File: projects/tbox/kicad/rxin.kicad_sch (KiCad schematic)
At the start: 24 parts, among them U601 OPA1678

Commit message: Annotate by board: KiCad annotator, first free after sheet number x100 (1xxx front, 2xxx control, 3xxx rear)
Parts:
- renumbered C601 to C3401, C602 to C3402, C618 to C3403, C619 to C3404, C622 to C3405, C623 to C3406, C614 to C3407, R601 to R3401, R605 to R3402, R635 to R3403, R636 to R3404, R602 to R3405, R606 to R3406, R633 to R3407, R634 to R3408, R603 to R3409, R607 to R3410, R604 to R3411, R608 to R3412, RV601 to RV3401, RV602 to RV3402, TP601 to TP3401, TP602 to TP3402, U601 to U3401

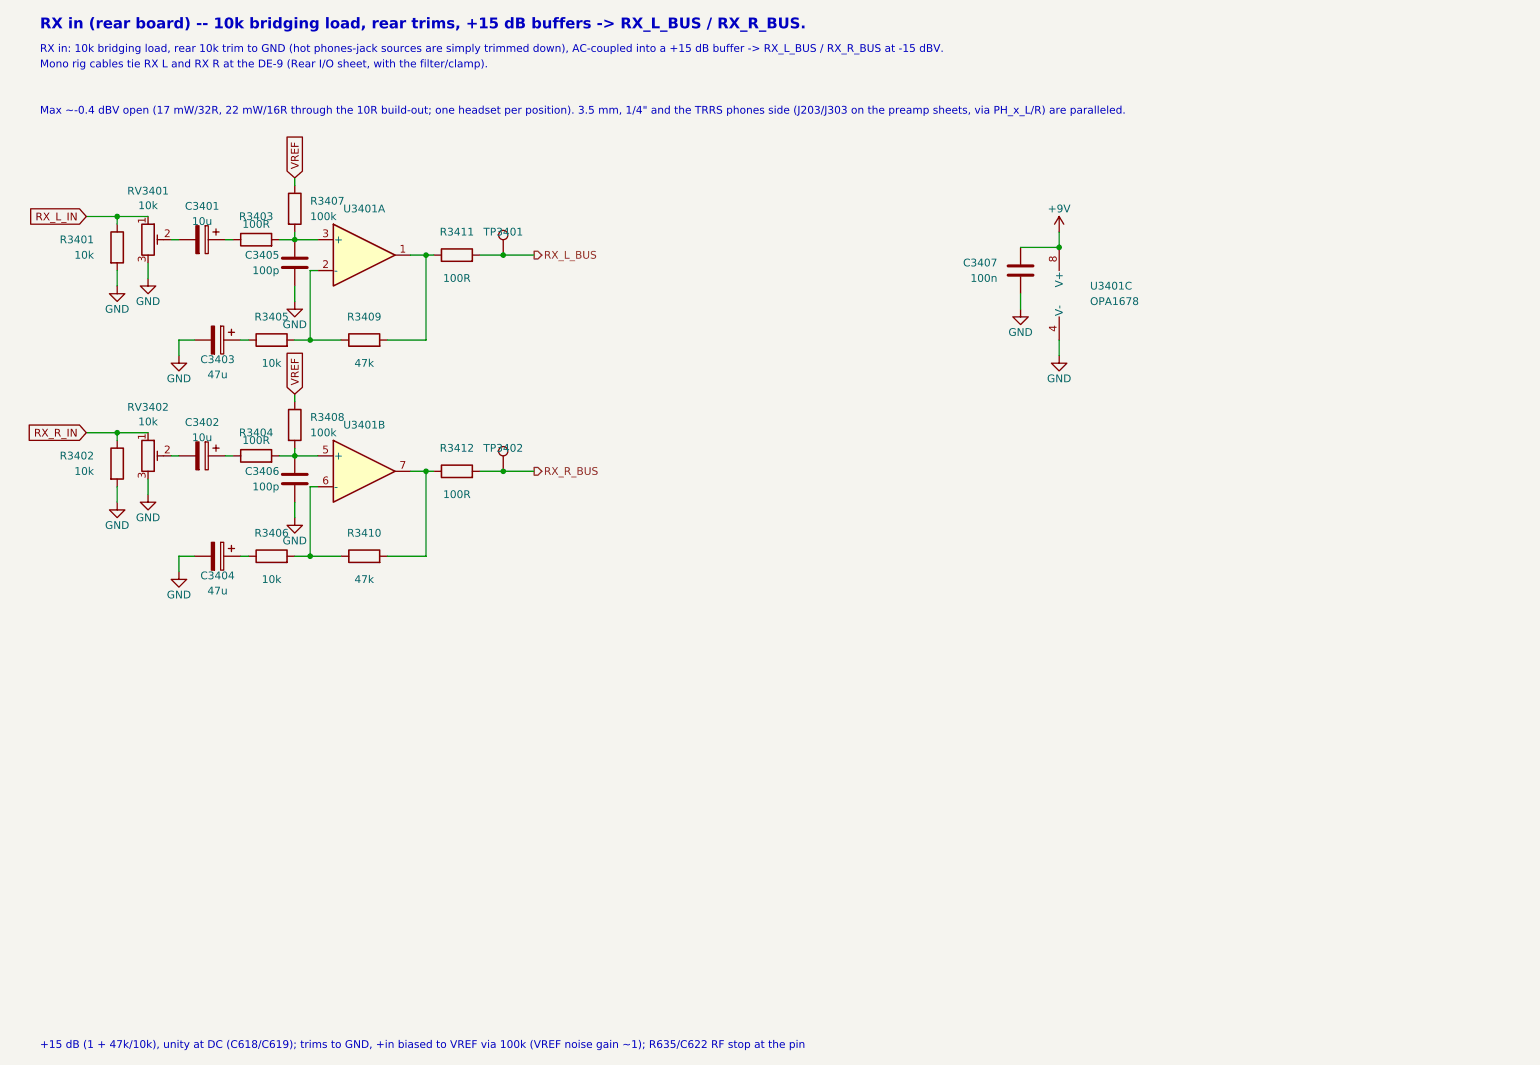
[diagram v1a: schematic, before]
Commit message: Rename refdes mentions in notes and docs to the board-coded numbering
Table-driven: the old->new map was derived from symbol UUIDs across the
annotation commit (619 instances, checked one-to-one and per board), and
only exact whole tokens from that table were replaced, in sheet notes,
connector Values, DESIGN.md, TODO.md and power_tree.json.  The one range
("J901-J904") and the one instance-specific ref in the shared Mute sheet
were rewritten by hand.  Power tree regenerated (loads now grouped by
board).  Netlist identical to the annotated baseline.
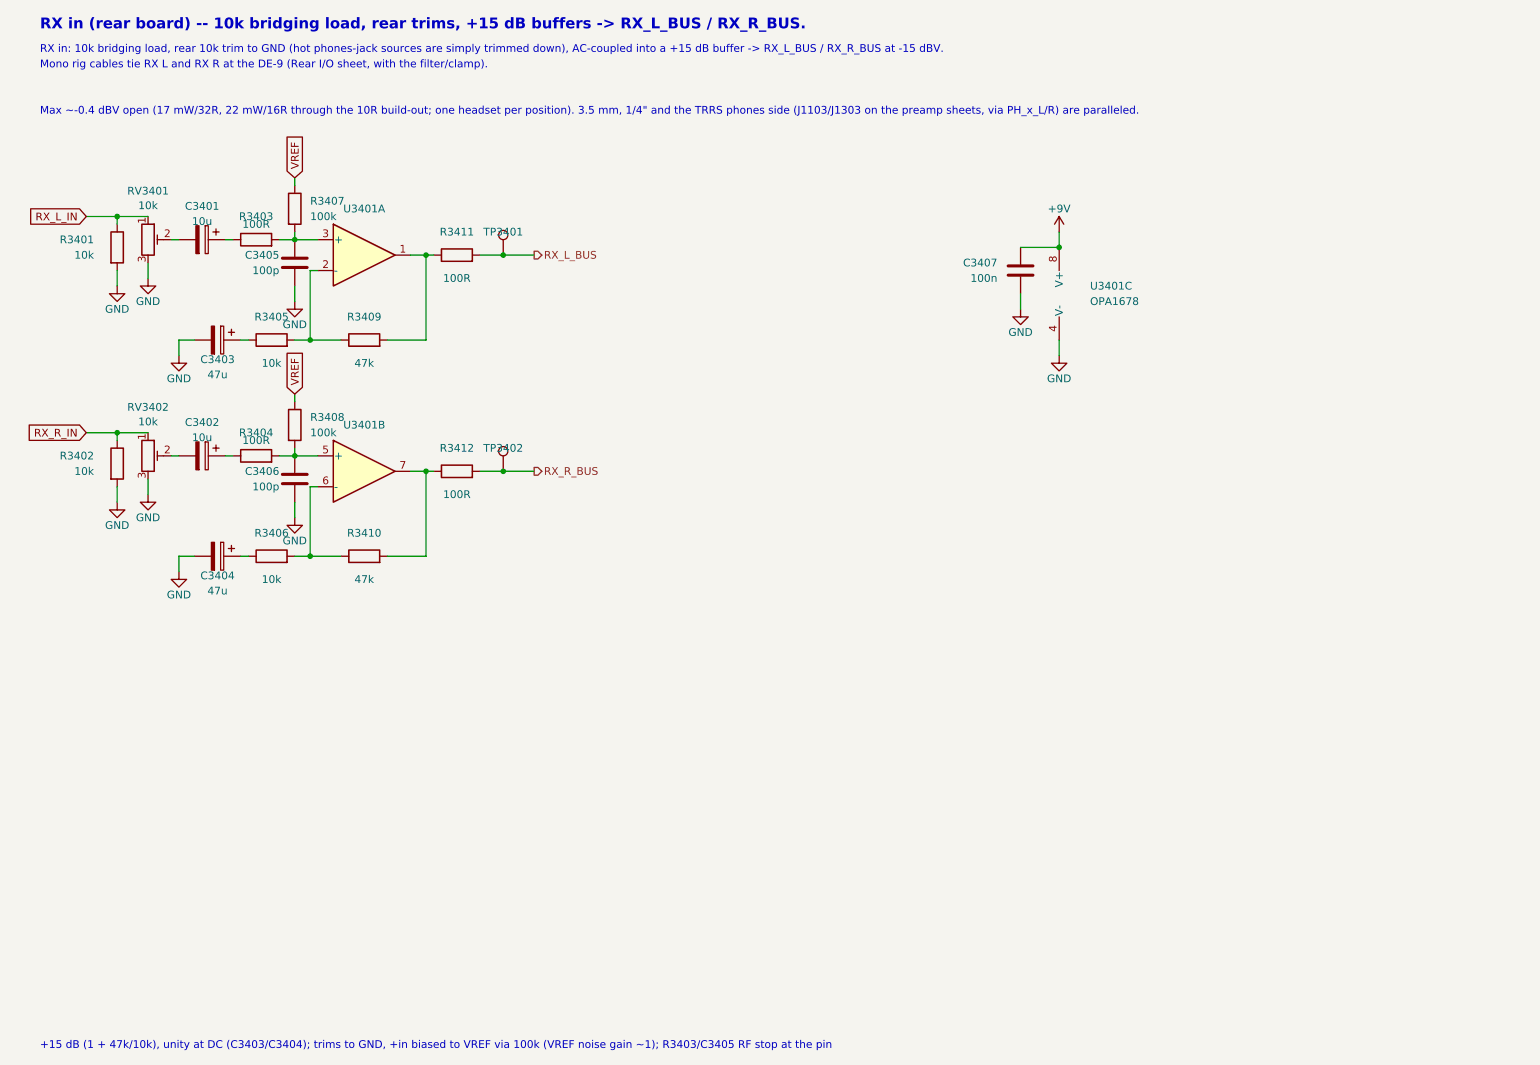
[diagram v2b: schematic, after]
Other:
- note added: "+15 dB (1 + 47k/10k), unity at DC (C3403/C3404); trims to GND, +in biased to VREF via 100k (VREF noise gain ~1); R3403/C3405 RF stop at the pin"
- note added: "Max ~-0.4 dBV open (17 mW/32R, 22 mW/16R through the 10R build-out; one headset per position). 3.5 mm, 1/4" and the TRRS phones side (J1103/J1303 on the preamp sheets, via PH_x_L/R) are paralleled."
- note removed: "+15 dB (1 + 47k/10k), unity at DC (C618/C619); trims to GND, +in biased to VREF via 100k (VREF noise gain ~1); R635/C622 RF stop at the pin"
- note removed: "Max ~-0.4 dBV open (17 mW/32R, 22 mW/16R through the 10R build-out; one headset per position). 3.5 mm, 1/4" and the TRRS phones side (J203/J303 on the preamp sheets, via PH_x_L/R) are paralleled."
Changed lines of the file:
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@@
 		(company "TBox")
 	)
-	(text "Max ~-0.4 dBV open (17 mW/32R, 22 mW/16R through the 10R build-out; one headset per position). 3.5 mm, 1/4\" and the TRRS phones side (J203/J303 on the preamp sheets, via PH_x_L/R) are paralleled."
+	(text "Max ~-0.4 dBV open (17 mW/32R, 22 mW/16R through the 10R build-out; one headset per position). 3.5 mm, 1/4\" and the TRRS phones side (J1103/J1303 on the preamp sheets, via PH_x_L/R) are paralleled."
 		(exclude_from_sim no)
 		(at 20.32 34.29 0)
@@
 		)
 	)
-	(text "+15 dB (1 + 47k/10k), unity at DC (C618/C619); trims to GND, +in biased to VREF via 100k (VREF noise gain ~1); R635/C622 RF stop at the pin"
+	(text "+15 dB (1 + 47k/10k), unity at DC (C3403/C3404); trims to GND, +in biased to VREF via 100k (VREF noise gain ~1); R3403/C3405 RF stop at the pin"
 		(exclude_from_sim no)
 		(at 20.32 187.96 0)

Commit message: Drop the fixed RX-input bridging resistors (R3401/R3402)
They sat in parallel with the 10k rear trims, so the input load was 5k
while LEVELS/DESIGN and the sheet note all said 10k.  The trim is the
bridging load.  Outcome of the "what can go" pass: test points, the
internal RF stoppers, the diode logic, the terminated spare op-amp
halves, both PTT jack sizes and the monitor buffers all stay, each for
a stated reason.
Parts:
- removed R3401, R3402: 10k, symbol Device:R
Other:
- note added: "RX in: the rear 10k trim to GND is the bridging load (hot phones-jack sources are simply trimmed down), AC-coupled into a +15 dB buffer -> RX_L_BUS / RX_R_BUS at -15 dBV."
- note removed: "RX in: 10k bridging load, rear 10k trim to GND (hot phones-jack sources are simply trimmed down), AC-coupled into a +15 dB buffer -> RX_L_BUS / RX_R_BUS at -15 dBV."

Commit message: Footprint pass: every board part has a footprint, chosen parts carry MPNs
0603 base for R and C <= 1 uF, 0805 for 4u7, 1206 for 10 uF ceramics
(including the three non-polar coupling caps), 1210 for the 47 uF X7R;
electrolytics by can size; Keystone 5015 test points.  Panel parts per
the discussion: Switchcraft 35RAPC(2A/2B)H3 and Neutrik NRJ6HM-1-PRE
where the sleeve must bond to the panel, CUI SJ1-353xNG and Rean
NRJ6HF-1 where it must not; Alpha 9 mm pots, Bourns 3386 side-adjust
trims, C&K 7101 AV2 / 7201 V-bracket toggles, C&K PVA buttons, IDC
2x13 headers (vertical on front/rear, right-angle on control), JST XH
for the Powerpole pigtail (through-hole on purpose), Triad TY-250P
transformers, 0805 LEDs with light pipes.  J3207 (GND post) is a
panel part: on_board no.

kicad/tbox.pretty holds the four footprints with no stock equivalent,
each drawn from the vendor drawing and saying so in its description:
Switchcraft 35RAPC__H3 (rev J), C&K 7101 AV2 and 7201 V-bracket
patterns, Triad TY-250P (pads mapped to the Transformer_1P_1S symbol,
6-7 tied on copper for 1:1).

tools/check_footprints.py enforces the invariant.  Netlist unchanged
apart from J3207 leaving the board.
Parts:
- C3401, C3402: footprint (none) -> Capacitor_SMD:CP_Elec_5x5.4
- C3403, C3404: footprint (none) -> Capacitor_SMD:CP_Elec_6.3x5.4
- C3405, C3406, C3407: footprint (none) -> Capacitor_SMD:C_0603_1608Metric
- R3403, R3404, R3405, R3406, R3407, R3408, R3409, R3410, R3411, R3412: footprint (none) -> Resistor_SMD:R_0603_1608Metric
- RV3401, RV3402: footprint (none) -> Potentiometer_THT:Potentiometer_Bourns_3386W_Horizontal; MPN (none) -> 3386W-1-103LF
- TP3401, TP3402: footprint (none) -> TestPoint:TestPoint_Keystone_5015_Micro_Mini; MPN (none) -> 5015
- U3401: footprint (none) -> Package_SO:SOIC-8_3.9x4.9mm_P1.27mm; MPN (none) -> OPA1678IDR
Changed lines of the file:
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@@
 			)
 		)
-		(property "Footprint" ""
+		(property "Footprint" "Resistor_SMD:R_0603_1608Metric"
 			(at 58.42 106.68 0)
 			(hide yes)
@@
 			)
 		)
-		(property "Footprint" ""
+		(property "Footprint" "Resistor_SMD:R_0603_1608Metric"
 			(at 58.42 71.12 0)
 			(hide yes)
@@
 			)
 		)
-		(property "Footprint" ""
+		(property "Footprint" "Capacitor_SMD:C_0603_1608Metric"
 			(at 62.23 93.98 0)
 			(hide yes)
@@
 			)
 		)
-		(property "Footprint" ""
+		(property "Footprint" "Resistor_SMD:R_0603_1608Metric"
 			(at 88.9 92.71 0)
 			(hide yes)
@@
 			)
 		)
-		(property "Footprint" ""
+		(property "Footprint" "Capacitor_SMD:CP_Elec_6.3x5.4"
 			(at 49.53 71.12 0)
 			(hide yes)
@@
 			)
 		)
-		(property "Footprint" ""
+		(property "Footprint" "Resistor_SMD:R_0603_1608Metric"
 			(at 62.23 85.09 0)
 			(hide yes)
@@
 			)
 		)
-		(property "Footprint" ""
+		(property "Footprint" "Capacitor_SMD:CP_Elec_6.3x5.4"
 			(at 49.53 106.68 0)
 			(hide yes)
@@
 			)
 		)
-		(property "Footprint" ""
+		(property "Footprint" "Potentiometer_THT:Potentiometer_Bourns_3386W_Horizontal"
 			(at 38.1 90.17 0)
 			(hide yes)
@@
 					(size 1.27 1.27)
 				)
+			)
+		)
+		(property "MPN" "3386W-1-103LF"
+			(at 38.1 90.17 0)
+			(effects
+				(font
+					(size 1.27 1.27)
+				)
+				(hide yes)
 			)
 		)
@@
 			)
 		)
-		(property "Footprint" ""
+		(property "Footprint" "TestPoint:TestPoint_Keystone_5015_Micro_Mini"
 			(at 96.52 57.15 0)
 			(hide yes)
@@
 					(size 1.27 1.27)
 				)
+			)
+		)
+		(property "MPN" "5015"
+			(at 96.52 57.15 0)
+			(effects
+				(font
+					(size 1.27 1.27)
+				)
+				(hide yes)
 			)
 		)
@@
 			)
 		)
-		(property "Footprint" ""
+		(property "Footprint" "Resistor_SMD:R_0603_1608Metric"
 			(at 73.66 106.68 0)
 			(hide yes)
@@
 			)
 		)
-		(property "Footprint" ""
+		(property "Footprint" "Package_SO:SOIC-8_3.9x4.9mm_P1.27mm"
 			(at 73.66 57.15 0)
 			(hide yes)
@@
 					(size 1.27 1.27)
 				)
+			)
+		)
+		(property "MPN" "OPA1678IDR"
+			(at 73.66 57.15 0)
+			(effects
+				(font
+					(size 1.27 1.27)
+				)
+				(hide yes)
 			)
 		)
@@
 			)
 		)
-		(property "Footprint" ""
+		(property "Footprint" "Package_SO:SOIC-8_3.9x4.9mm_P1.27mm"
 			(at 190.5 63.5 0)
 			(hide yes)
@@
 					(size 1.27 1.27)
 				)
+			)
+		)
+		(property "MPN" "OPA1678IDR"
+			(at 190.5 63.5 0)
+			(effects
+				(font
+					(size 1.27 1.27)
+				)
+				(hide yes)
 			)
 		)
@@
 			)
 		)
-		(property "Footprint" ""
+		(property "Footprint" "Capacitor_SMD:C_0603_1608Metric"
 			(at 62.23 58.42 0)
 			(hide yes)
@@
 			)
 		)
-		(property "Footprint" ""
+		(property "Footprint" "Package_SO:SOIC-8_3.9x4.9mm_P1.27mm"
 			(at 73.66 92.71 0)
 			(hide yes)
@@
 					(size 1.27 1.27)
 				)
+			)
+		)
+		(property "MPN" "OPA1678IDR"
+			(at 73.66 92.71 0)
+			(effects
+				(font
+					(size 1.27 1.27)
+				)
+				(hide yes)
 			)
 		)
@@
 			)
 		)
-		(property "Footprint" ""
+		(property "Footprint" "Resistor_SMD:R_0603_1608Metric"
 			(at 55.88 90.17 0)
 			(hide yes)
@@
 			)
 		)
-		(property "Footprint" ""
+		(property "Footprint" "Resistor_SMD:R_0603_1608Metric"
 			(at 62.23 49.53 0)
 			(hide yes)
@@
 			)
 		)
-		(property "Footprint" ""
+		(property "Footprint" "Resistor_SMD:R_0603_1608Metric"
 			(at 88.9 57.15 0)
 			(hide yes)
@@
 			)
 		)
-		(property "Footprint" ""
+		(property "Footprint" "Potentiometer_THT:Potentiometer_Bourns_3386W_Horizontal"
 			(at 38.1 54.61 0)
 			(hide yes)
@@
 					(size 1.27 1.27)
 				)
+			)
+		)
+		(property "MPN" "3386W-1-103LF"
+			(at 38.1 54.61 0)
+			(effects
+				(font
+					(size 1.27 1.27)
+				)
+				(hide yes)
 			)
 		)
@@
 			)
 		)
-		(property "Footprint" ""
+		(property "Footprint" "Capacitor_SMD:CP_Elec_5x5.4"
 			(at 46.99 54.61 0)
 			(hide yes)
@@
 			)
 		)
-		(property "Footprint" ""
+		(property "Footprint" "Capacitor_SMD:C_0603_1608Metric"
 			(at 181.61 59.69 0)
 			(hide yes)
@@
 			)
 		)
-		(property "Footprint" ""
+		(property "Footprint" "Resistor_SMD:R_0603_1608Metric"
 			(at 55.88 54.61 0)
 			(hide yes)
@@
 			)
 		)
-		(property "Footprint" ""
+		(property "Footprint" "Capacitor_SMD:CP_Elec_5x5.4"
 			(at 46.99 90.17 0)
 			(hide yes)
@@
 			)
 		)
-		(property "Footprint" ""
+		(property "Footprint" "TestPoint:TestPoint_Keystone_5015_Micro_Mini"
 			(at 96.52 92.71 0)
 			(hide yes)
@@
 					(size 1.27 1.27)
 				)
+			)
+		)
+		(property "MPN" "5015"
+			(at 96.52 92.71 0)
+			(effects
+				(font
+					(size 1.27 1.27)
+				)
+				(hide yes)
 			)
 		)
@@
 			)
 		)
-		(property "Footprint" ""
+		(property "Footprint" "Resistor_SMD:R_0603_1608Metric"
 			(at 73.66 71.12 0)
 			(hide yes)
